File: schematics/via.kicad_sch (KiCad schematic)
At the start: 28 parts, among them SW2 SW_DIP_x08, U16 74HC14, U17 W65C22SxP

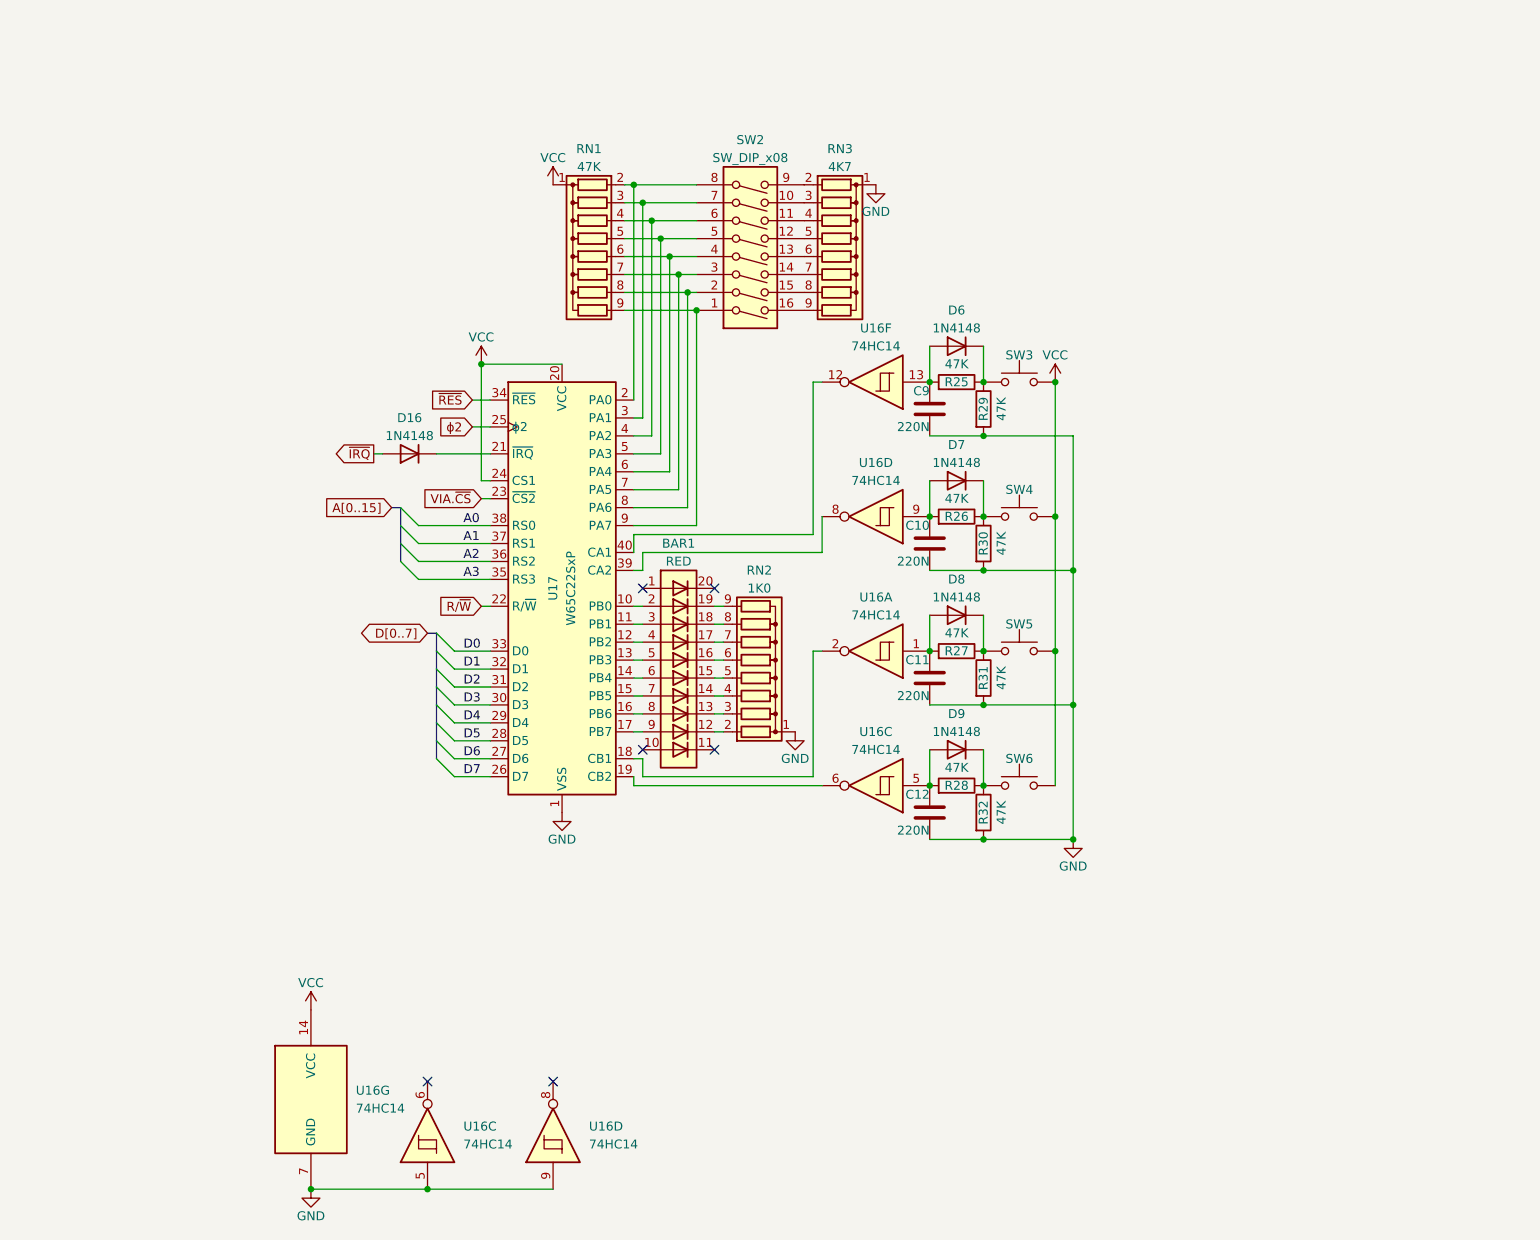
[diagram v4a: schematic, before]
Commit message: my keyboard needed a transceiver after all :(
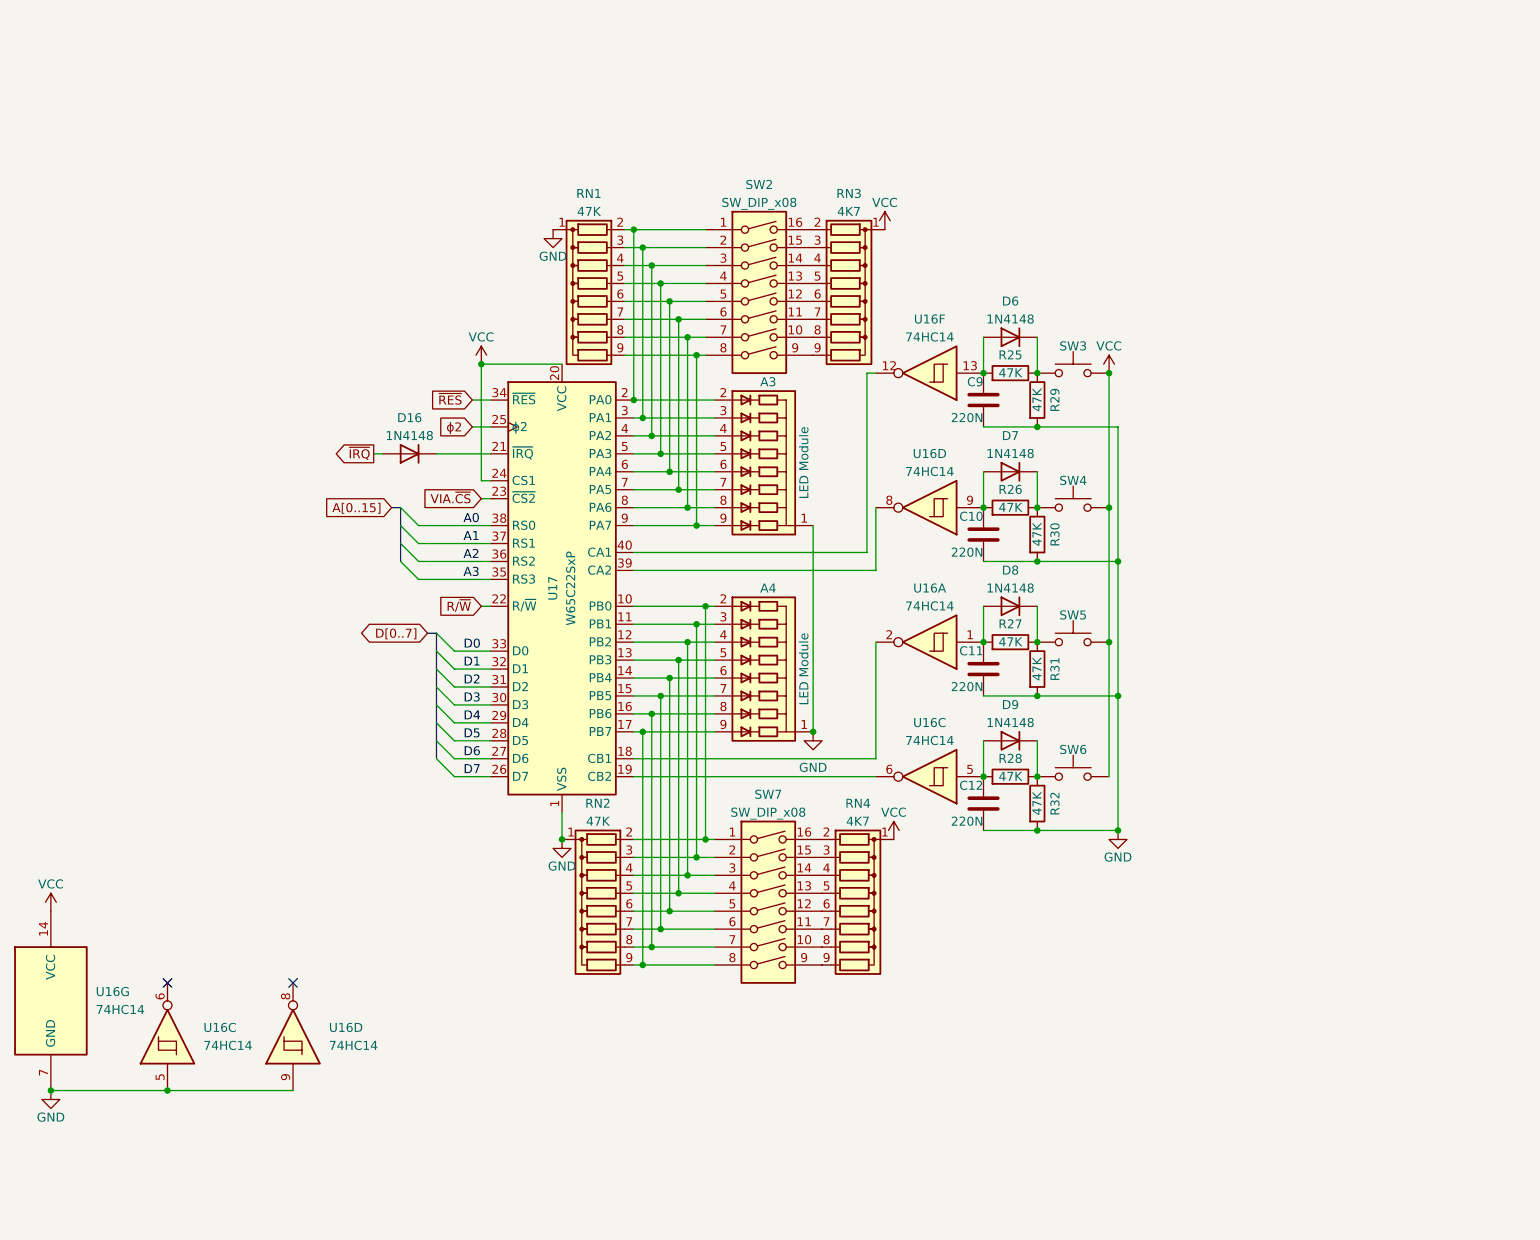
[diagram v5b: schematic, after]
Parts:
- removed BAR1: RED, Display:HDSP-4830, symbol LED:HDSP-4830_2
- added A3, A4: LED Module, symbol bv6502_hw:LED_Module
- added RN4: 4K7, Resistor_THT:R_Array_SIP9, symbol Device:R_Network08
- added SW7: SW_DIP_x08, symbol Switch:SW_DIP_x08
- RN2: value 1K0 -> 47K
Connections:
- net GND: now also RN1.1 (common), A3.1, A4.1; no longer RN3.1 (common)
- net VCC: now also RN3.1 (common), RN4.1 (common); no longer RN1.1 (common)
- net at RN2.2 (R1): now also U17.10 (PB0), A4.2, SW7.1
- net at RN2.3 (R2): now also U17.11 (PB1), A4.3, SW7.2
- net at RN2.4 (R3): now also U17.12 (PB2), A4.4, SW7.3
- net at RN2.5 (R4): now also U17.13 (PB3), A4.5, SW7.4
- net at RN2.6 (R5): now also U17.14 (PB4), A4.6, SW7.5
- net at RN2.7 (R6): now also U17.15 (PB5), A4.7, SW7.6
- net at RN2.8 (R7): now also U17.16 (PB6), A4.8, SW7.7
- net at RN2.9 (R8): now also U17.17 (PB7), A4.9, SW7.8
- net at RN1.2 (R1), U17.2 (PA0): now also SW2.1, A3.2; no longer SW2.8
- net at RN1.3 (R2), U17.3 (PA1): now also SW2.2, A3.3; no longer SW2.7
- net at RN1.4 (R3), U17.4 (PA2): now also SW2.3, A3.4; no longer SW2.6
- net at RN1.5 (R4), U17.5 (PA3): now also SW2.4, A3.5; no longer SW2.5
- net at RN1.6 (R5), U17.6 (PA4): now also SW2.5, A3.6; no longer SW2.4
- net at RN1.7 (R6), U17.7 (PA5): now also SW2.6, A3.7; no longer SW2.3
- net at RN1.8 (R7), U17.8 (PA6): now also SW2.7, A3.8; no longer SW2.2
- net at RN1.9 (R8), U17.9 (PA7): now also SW2.8, A3.9; no longer SW2.1
- net at SW2.10: now also RN3.8 (R7); no longer RN3.3 (R2)
- net at SW2.11: now also RN3.7 (R6); no longer RN3.4 (R3)
- net at SW2.12: now also RN3.6 (R5); no longer RN3.5 (R4)
- net at SW2.13: now also RN3.5 (R4); no longer RN3.6 (R5)
- net at SW2.14: now also RN3.4 (R3); no longer RN3.7 (R6)
- net at SW2.15: now also RN3.3 (R2); no longer RN3.8 (R7)
- net at SW2.16: now also RN3.2 (R1); no longer RN3.9 (R8)
- net at SW2.9: now also RN3.9 (R8); no longer RN3.2 (R1)
- new net: RN4.2 (R1), SW7.16
- new net: RN4.3 (R2), SW7.15
- new net: RN4.4 (R3), SW7.14
- new net: RN4.5 (R4), SW7.13
- new net: RN4.6 (R5), SW7.12
- new net: RN4.7 (R6), SW7.11
- new net: RN4.8 (R7), SW7.10
- new net: RN4.9 (R8), SW7.9
- no-connect marks 6 -> 2
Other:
- moved on the sheet: C10, C11, C12, C9, D6, D7, D8, D9, R25, R26, R27, R28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
